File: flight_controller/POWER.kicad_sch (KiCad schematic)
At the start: 3 parts, among them J12 CNJMA2012WV-S-10P

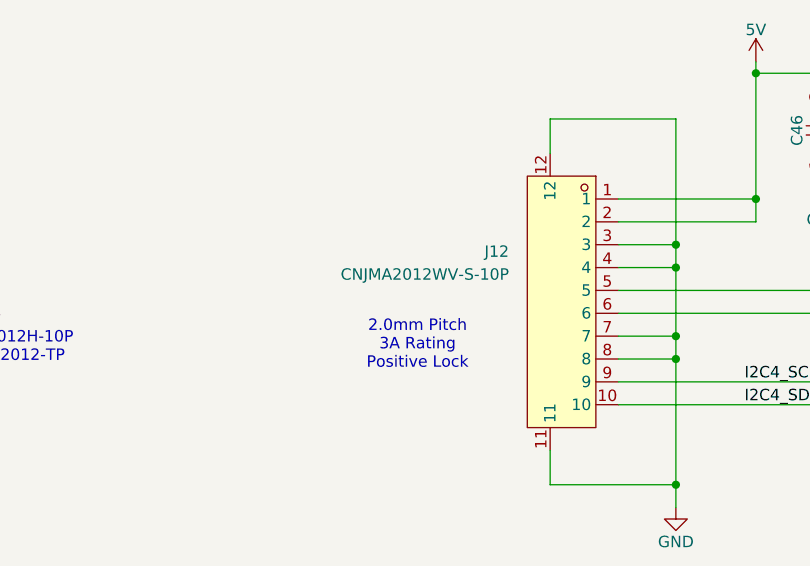
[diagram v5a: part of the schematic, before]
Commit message: Replace power connector
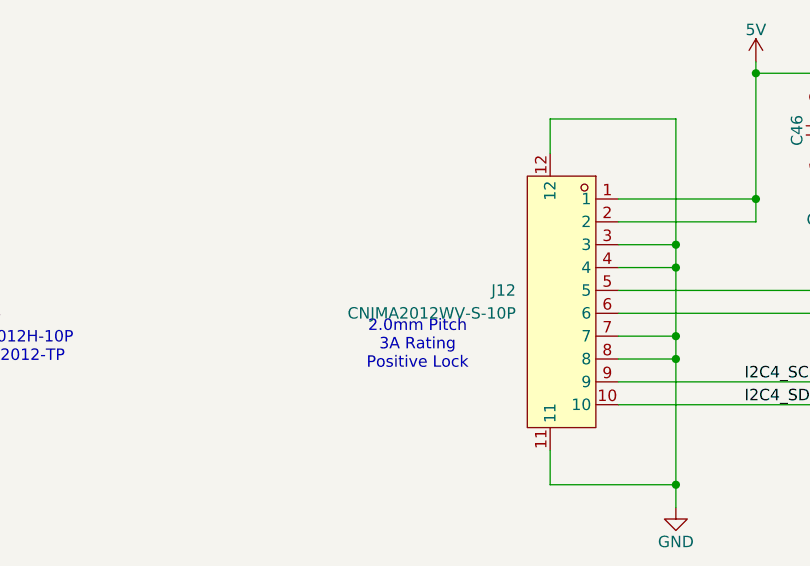
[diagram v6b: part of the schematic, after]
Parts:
- removed J12: CNJMA2012WV-S-10P, easyeda2kicad:CONN-SMD_10P-P1.25_CNJM_CNJMA2012WV-S-10P, symbol lampelKicadLIB:CNJMA2012WV-S-10P
- added J12: CNJMA2012WV-S-10P, easyeda2kicad:CONN-SMD_10P-P2.00_CNJM_CNJMA2012WV-S-10P, symbol easyeda_lampel:CNJMA2012WV-S-10P
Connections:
- net 3V3: now also J12.5, J12.6
- net 5V: now also J12.1, J12.2
- net GND: now also J12.11, J12.12, J12.3, J12.4, J12.7, J12.8
- net I2C4_SCL_INA226: now also J12.9
- net I2C4_SDA_INA226: now also J12.10
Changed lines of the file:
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@@
-	)
-	(symbol
-		(lib_id "lampelKicadLIB:CNJMA2012WV-S-10P")
-		(at 123.19 90.17 0)
-		(mirror y)
-		(unit 1)
-		(exclude_from_sim no)
-		(in_bom yes)
-		(on_board yes)
-		(dnp no)
-		(property "Reference" "J12"
-			(at 116.078 84.5819 0)
-			(effects
-				(font
-					(size 1.27 1.27)
-				)
-				(justify left)
-			)
-		)
-		(property "Value" "CNJMA2012WV-S-10P"
-			(at 116.078 87.1219 0)
-			(effects
-				(font
-					(size 1.27 1.27)
-				)
-				(justify left)
-			)
-		)
-		(property "Footprint" "easyeda2kicad:CONN-SMD_10P-P1.25_CNJM_CNJMA2012WV-S-10P"
-			(at 123.19 114.3 0)
-			(effects
-				(font
-					(size 1.27 1.27)
-				)
-				(hide yes)
-			)
-		)
-		(property "Datasheet" "https://www.lcsc.com/product-detail/C5151225.html"
-			(at 123.19 100.33 0)
-			(effects
-				(font
-					(size 1.27 1.27)
-				)
-				(hide yes)
-			)
-		)
-		(property "Description" "1 -25℃~+85℃ 10P 10 2mm 3A 250V 1x10P SMD,P=2mm Headers, Male Pins RoHS"
-			(at 123.19 90.17 0)
-			(effects
-				(font
-					(size 1.27 1.27)
-				)
-				(hide yes)
-			)
-		)
-		(property "LCSC Part" "C5151225"
-			(at 123.19 116.84 0)
-			(effects
-				(font
-					(size 1.27 1.27)
-				)
-				(hide yes)
-			)
-		)
-		(pin "8"
-		)
-		(pin "7"
-		)
-		(pin "1"
-		)
-		(pin "12"
-		)
-		(pin "3"
-		)
-		(pin "4"
-		)
-		(pin "6"
-		)
-		(pin "5"
-		)
-		(pin "9"
-		)
-		(pin "2"
-		)
-		(pin "10"
-		)
-		(pin "11"
-		)
-		(instances
-			(project ""
-				(path "/17737359-1a8e-4237-8899-d9604030bc1d/04e8a37e-c803-4b03-9bae-b305438bfc27"
-					(reference "J12")
-					(unit 1)
-				)
-			)
-		)
 	)
 	(symbol
@@
 					(unit 1)
 				)
+			)
+		)
+	)
+	(symbol
+		(lib_id "easyeda_lampel:CNJMA2012WV-S-10P")
+		(at 123.19 90.17 0)
+		(mirror y)
+		(unit 1)
+		(exclude_from_sim no)
+		(in_bom yes)
+		(on_board yes)
+		(dnp no)
+		(fields_autoplaced yes)
+		(property "Reference" "J12"
+			(at 116.84 88.8999 0)
+			(effects
+				(font
+					(size 1.27 1.27)
+				)
+				(justify left)
+			)
+		)
+		(property "Value" "CNJMA2012WV-S-10P"
+			(at 116.84 91.4399 0)
+			(effects
+				(font
+					(size 1.27 1.27)
+				)
+				(justify left)
+			)
+		)
+		(property "Footprint" "easyeda2kicad:CONN-SMD_10P-P2.00_CNJM_CNJMA2012WV-S-10P"
+			(at 123.19 114.3 0)
+			(effects
+				(font
+					(size 1.27 1.27)
+				)
+				(hide yes)
+			)
+		)
+		(property "Datasheet" "https://www.lcsc.com/product-detail/C5151225.html"
+			(at 123.19 100.33 0)
+			(effects
+				(font
+					(size 1.27 1.27)
+				)
+				(hide yes)
+			)
+		)
+		(property "Description" "1 -25℃~+85℃ 10P 10 2mm 3A 250V 1x10P SMD,P=2mm Headers, Male Pins RoHS"
+			(at 123.19 90.17 0)
+			(effects
+				(font
+					(size 1.27 1.27)
+				)
+				(hide yes)
+			)
+		)
+		(property "LCSC Part" "C5151225"
+			(at 123.19 116.84 0)
+			(effects
+				(font
+					(size 1.27 1.27)
+				)
+				(hide yes)
+			)
+		)
+		(pin "8"
+		)
+		(pin "2"
+		)
+		(pin "5"
+		)
+		(pin "1"
+		)
+		(pin "6"
+		)
+		(pin "7"
+		)
+		(pin "4"
+		)
+		(pin "3"
+		)
+		(pin "11"
+		)
+		(pin "9"
+		)
+		(pin "10"
+		)
+		(pin "12"
+		)
+		(instances
+			(project ""
+				(path "/17737359-1a8e-4237-8899-d9604030bc1d/04e8a37e-c803-4b03-9bae-b305438bfc27"
+					(reference "J12")
+					(unit 1)
+				)

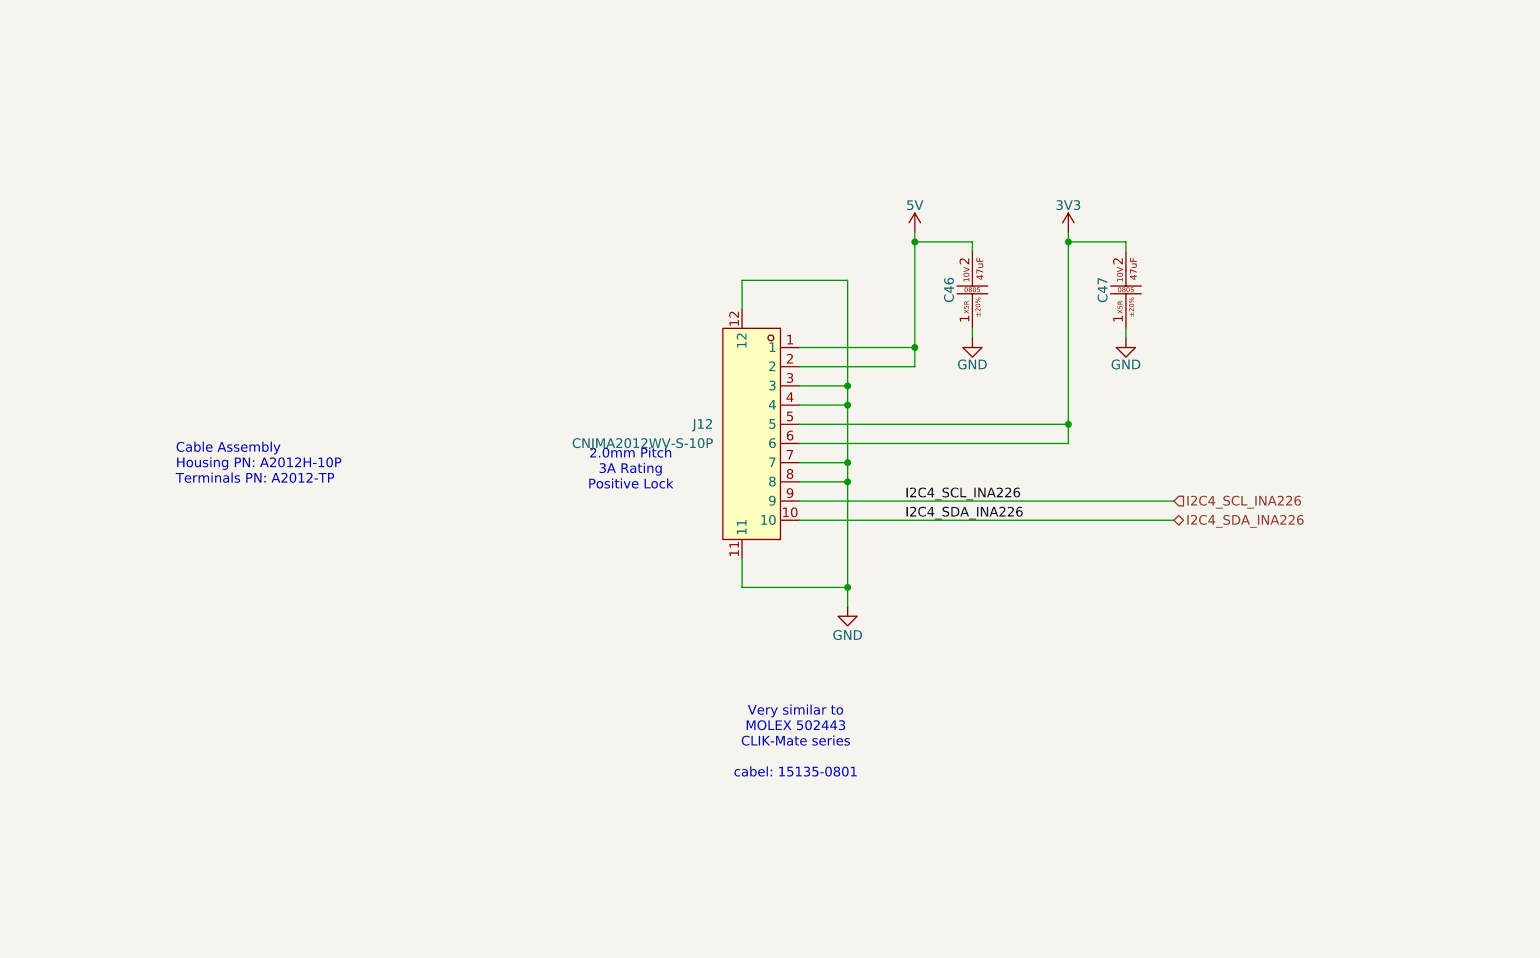
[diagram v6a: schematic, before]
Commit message: Fixed 10pin and pushed to pcb
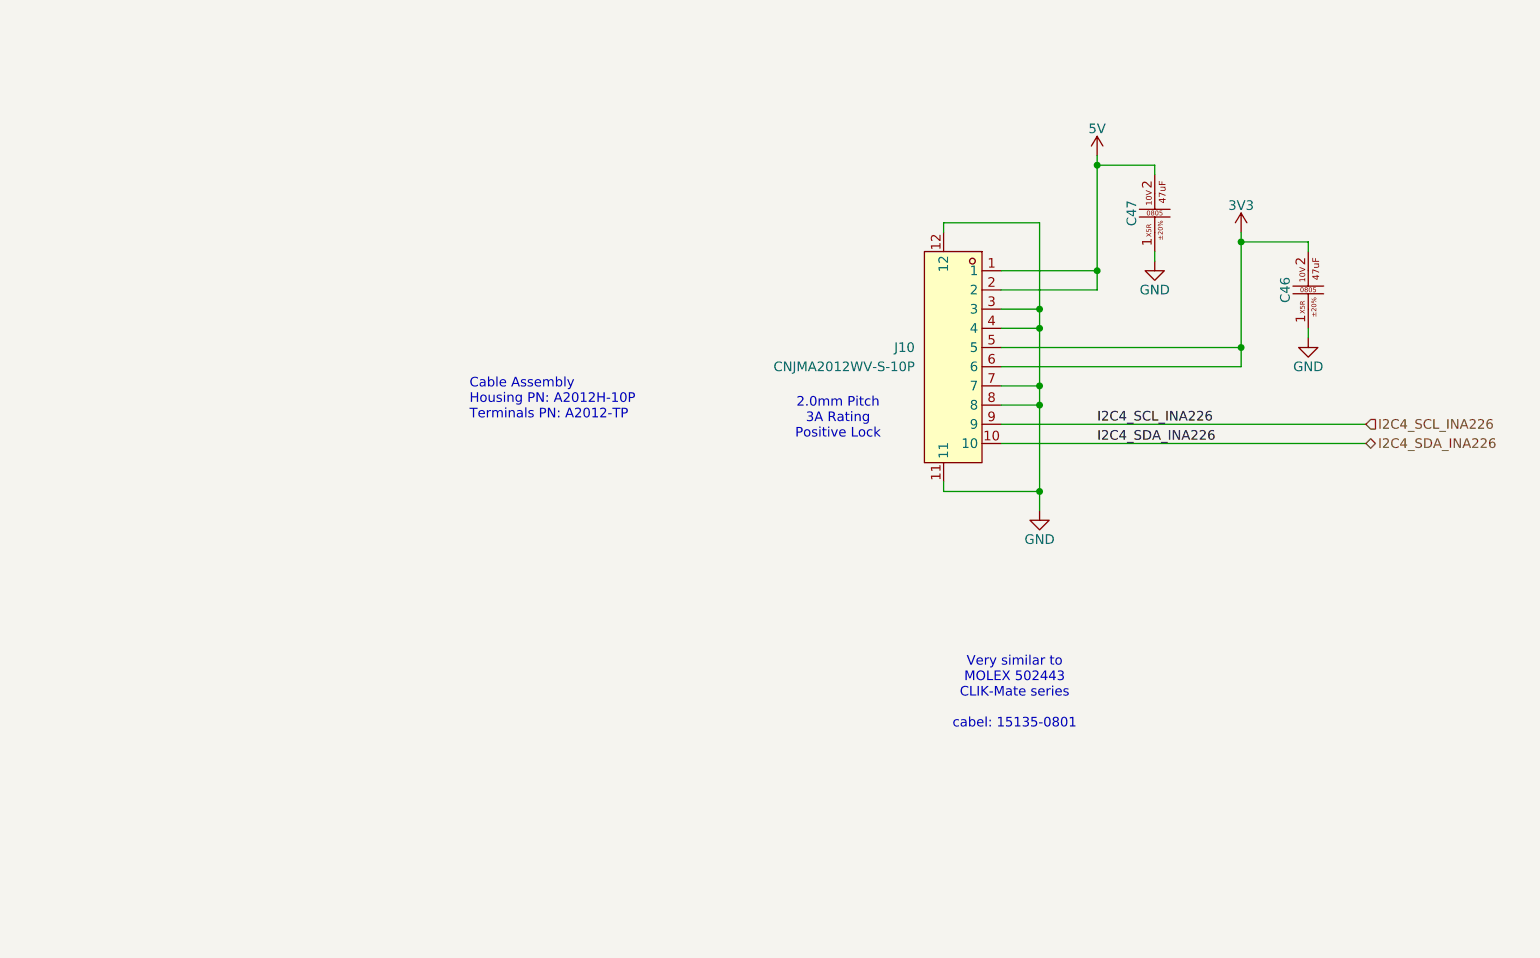
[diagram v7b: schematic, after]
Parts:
- removed J12: CNJMA2012WV-S-10P, easyeda2kicad:CONN-SMD_10P-P2.00_CNJM_CNJMA2012WV-S-10P, symbol easyeda_lampel:CNJMA2012WV-S-10P
- added J10: CNJMA2012WV-S-10P, easyeda2kicad:CONN-SMD_10P-P2.00_CNJM_CNJMA2012WV-S-10P, symbol lampelKicadLIB:CNJMA2012WV-S-10P
- renumbered C47 to C46, C46 to C47
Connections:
- net 3V3: now also J10.5, J10.6
- net 5V: now also J10.1, J10.2
- net GND: now also J10.11, J10.12, J10.3, J10.4, J10.7, J10.8
- net I2C4_SCL_INA226: now also J10.9
- net I2C4_SDA_INA226: now also J10.10
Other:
- moved on the sheet: C46, C47

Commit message: Revert to state of commit 2458262 moved all to components to top
Reverts commits: d012532, 3d9c600, 58bc0ac
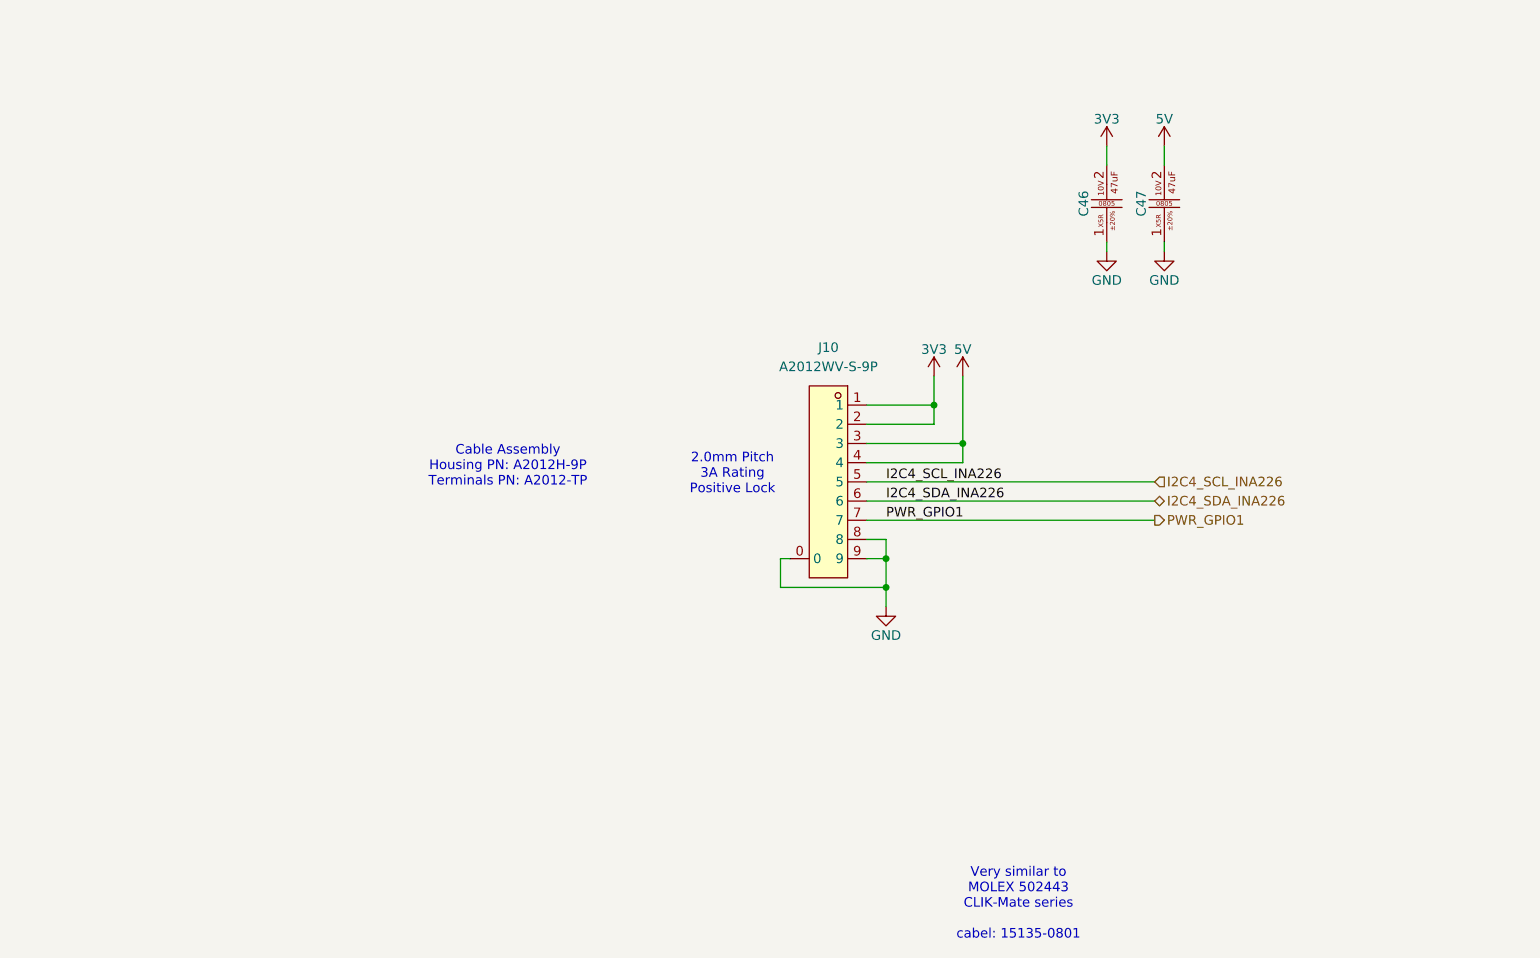
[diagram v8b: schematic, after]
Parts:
- removed J10: CNJMA2012WV-S-10P, easyeda2kicad:CONN-SMD_10P-P2.00_CNJM_CNJMA2012WV-S-10P, symbol lampelKicadLIB:CNJMA2012WV-S-10P
- added J10: A2012WV-S-9P, easyeda2kicad:CONN-SMD_A2012WV-S-9P, symbol lampelKicadLIB:A2012WV-S-9P
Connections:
- net 3V3: now also J10.1, J10.2
- net 5V: now also J10.3, J10.4
- net GND: now also J10.0, J10.8, J10.9
- net I2C4_SCL_INA226: now also J10.5
- net I2C4_SDA_INA226: now also J10.6
- new net PWR_GPIO1: J10.7
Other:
- note added: "Cable Assembly Housing PN: A2012H-9P Terminals PN: A2012-TP"
- note removed: "Cable Assembly Housing PN: A2012H-10P Terminals PN: A2012-TP"
- moved on the sheet: C46, C47
